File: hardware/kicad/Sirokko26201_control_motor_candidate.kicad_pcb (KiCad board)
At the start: 2 copper layers, 335 x 170 mm, 158 parts, among them J1 DEVKITC1_J1, J10 TC_K_EXHAUST_T+_T-, J102 MOTOR_24V_HIGH_SPEED; 125W_HE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, J11 TC_K_AIR_T+_T-, J12 ROOM_DS18B20_HARNESS, J13 24V_INPUT_PHOENIX_1756993_WIP, J22 START_STOP B3F-4055 + B32-138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, J23 ENCODER EC11E15244G1 + KNOB 4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, J24 RESET NKK BB25AB-FA, J26 TFT CABLE HARWIN M20-9960845 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, J27 GLOW_OUTPUT_PHOENIX_1756993, J28 CLUTCH_OUTPUT_PHOENIX_1756993, J3 DEVKITC1_J3, K1 DG85BM-5021-76-1024 + DZ85AB-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, K2 DG85BM-5021-76-1024 + DZ85AB-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, K3 DG85BM-5021-76-1024 + DZ85AB-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, Q1 IPB017N10N5LFATMA1 WIP, Q101 IRFB4110PBF (100V; RDS(on) @ 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, Q2 IPB017N10N5LFATMA1 WIP, Q20 BC847B,215, Q3 IPB017N10N5LFATMA1 WIP, Q4 IPB017N10N5LFATMA1 WIP, U1 TPS3431SDRBR, U10 MAX31856MUD+, U101 LM5013DDAR, U11 DRV8803PWPR, U13 LM74800QDRRRQ1 WIP_NOT_TRANSI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, U2 SN74HCS74D, U20 SN74LVC1G97DBVR, U301 TPS62162DSGR, U302 TPS3808G33DBVR, U303 74LVC125APW,118 Nexperia ONLY, U6 SN74HCS11D, U9 MAX31856MUD+, U9001 LTC7001IMSE#PBF; MSOP-10 EP, U9002 INA240A1ID, U9003 TLV9020DBVR, U9004 SN74LVC1G32DBVR, U9005 SN74LVC1G08DBVR, U9006 SN74LVC1G08DBVR, U9007 LM317HVT/NOPB TO-220; TJ 0…12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

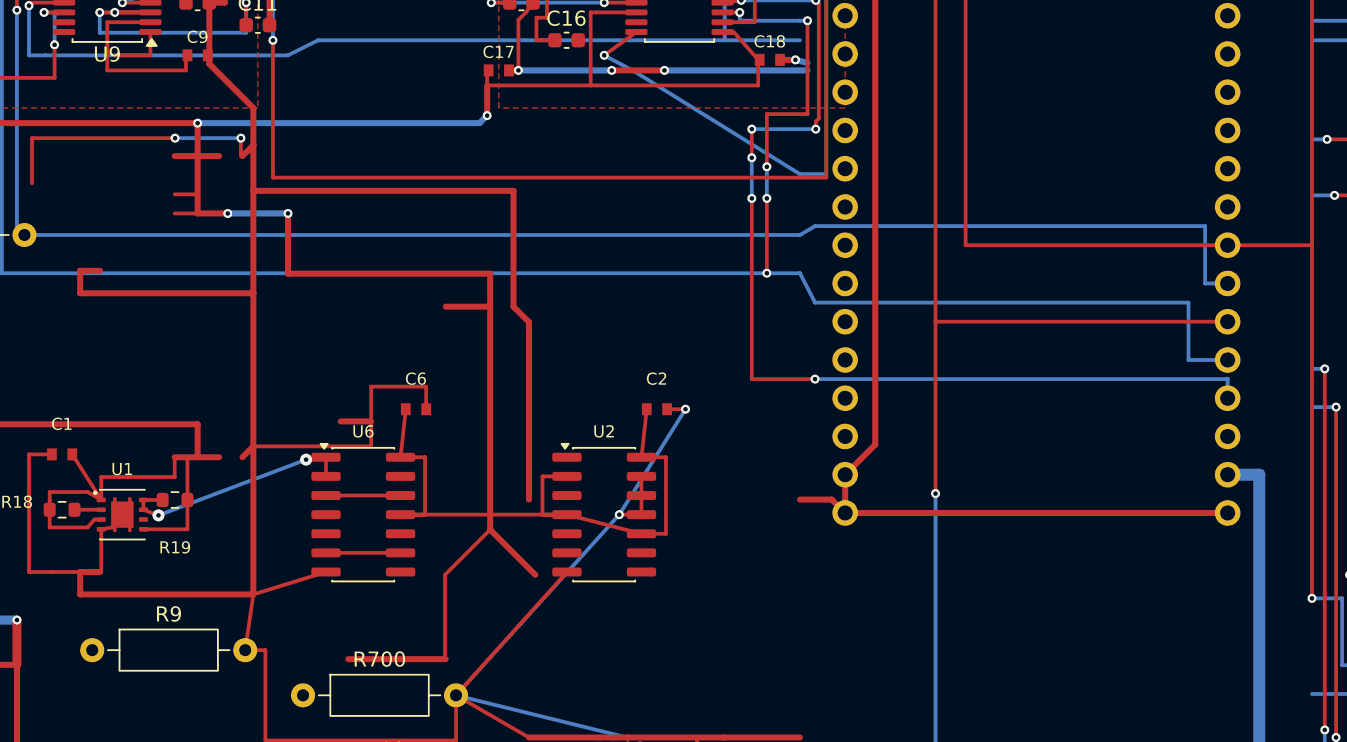
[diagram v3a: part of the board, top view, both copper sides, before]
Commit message: Route WD_HEARTBEAT and CLEAR_N
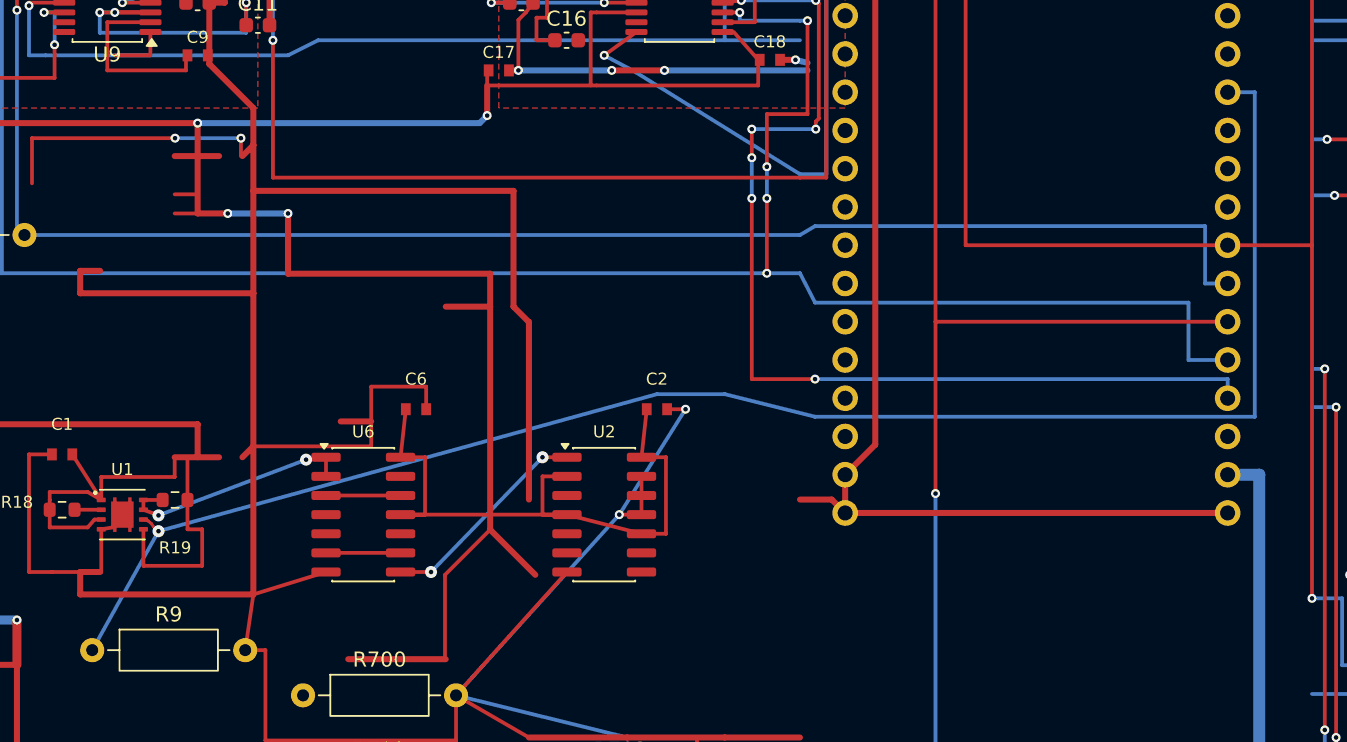
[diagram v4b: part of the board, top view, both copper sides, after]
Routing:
- net /WD_HEARTBEAT: track 0.00 -> 107.9 mm, vias 0 -> 1
- net /MinimalSafety/CLEAR_N: track 0.00 -> 14.3 mm, vias 0 -> 2
- net /+3V3: track 1320.8 -> 1327.6 mm
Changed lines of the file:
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@@
 	)
 	(segment
-		(start 32.4 65.975)
-		(end 35.325 65.975)
-		(width 0.25)
-		(layer "F.Cu")
-		(net "/+3V3")
-	)
-	(segment
 		(start 18 42.77)
 		(end 18 39)
@@
 		(net "/EN_CHIP_PU")
 	)
+	(segment
+		(start 29 74)
+		(end 33.4 66.1)
+		(width 0.25)
+		(layer "B.Cu")
+		(net "/WD_HEARTBEAT")
+	)
+	(segment
+		(start 33.4 66.1)
+		(end 66.5 57)
+		(width 0.25)
+		(layer "B.Cu")
+		(net "/WD_HEARTBEAT")
+	)
+	(segment
+		(start 66.5 57)
+		(end 71 57)
+		(width 0.25)
+		(layer "B.Cu")
+		(net "/WD_HEARTBEAT")
+	)
+	(segment
+		(start 71 57)
+		(end 77 58.5)
+		(width 0.25)
+		(layer "B.Cu")
+		(net "/WD_HEARTBEAT")
+	)
+	(segment
+		(start 77 58.5)
+		(end 106.2 58.5)
+		(width 0.25)
+		(layer "B.Cu")
+		(net "/WD_HEARTBEAT")
+	)
+	(segment
+		(start 106.2 58.5)
+		(end 106.2 36.95)
+		(width 0.25)
+		(layer "B.Cu")
+		(net "/WD_HEARTBEAT")
+	)
+	(segment
+		(start 106.2 36.95)
+		(end 104.4 36.95)
+		(width 0.25)
+		(layer "B.Cu")
+		(net "/WD_HEARTBEAT")
+	)
+	(segment
+		(start 32.4 65.975)
+		(end 32.4 68.4)
+		(width 0.25)
+		(layer "F.Cu")
+		(net "/+3V3")
+	)
+	(segment
+		(start 32.4 68.4)
+		(end 36.3 68.4)
+		(width 0.25)
+		(layer "F.Cu")
+		(net "/+3V3")
+	)
+	(segment
+		(start 36.3 68.4)
+		(end 36.3 65.975)
+		(width 0.25)
+		(layer "F.Cu")
+		(net "/+3V3")
+	)
+	(segment
+		(start 36.3 65.975)
+		(end 35.325 65.975)
+		(width 0.25)
+		(layer "F.Cu")
+		(net "/+3V3")
+	)
+	(segment
+		(start 32.4 65.325)
+		(end 32.72 65.42)
+		(width 0.2)
+		(layer "F.Cu")
+		(net "/WD_HEARTBEAT")
+	)
+	(segment
+		(start 32.72 65.42)
+		(end 32.915465 65.582988)
+		(width 0.2)
+		(layer "F.Cu")
+		(net "/WD_HEARTBEAT")
+	)
+	(segment
+		(start 32.915465 65.582988)
+		(end 33.08 65.82)
+		(width 0.2)
+		(layer "F.Cu")
+		(net "/WD_HEARTBEAT")
+	)
+	(segment
+		(start 33.08 65.82)
+		(end 33.4 66.1)
+		(width 0.2)
+		(layer "F.Cu")
+		(net "/WD_HEARTBEAT")
+	)
+	(via
+		(at 33.4 66.1)
+		(size 0.8)
+		(drill 0.3)
+		(layers "F.Cu" "B.Cu")
+		(net "/WD_HEARTBEAT")
+	)
+	(segment
+		(start 49.475 68.81)
+		(end 51.5 68.81)
+		(width 0.25)
+		(layer "F.Cu")
+		(net "/MinimalSafety/CLEAR_N")
+	)
+	(via
+		(at 51.5 68.81)
+		(size 0.8)
+		(drill 0.3)
+		(layers "F.Cu" "B.Cu")
+		(net "/MinimalSafety/CLEAR_N")
+	)
+	(segment
+		(start 51.5 68.81)
+		(end 58.9 61.19)
+		(width 0.25)
+		(layer "B.Cu")
+		(net "/MinimalSafety/CLEAR_N")
+	)
+	(via
+		(at 58.9 61.19)
+		(size 0.8)
+		(drill 0.3)
+		(layers "F.Cu" "B.Cu")
+		(net "/MinimalSafety/CLEAR_N")
+	)
+	(segment
+		(start 58.9 61.19)
+		(end 60.525 61.19)
+		(width 0.25)
+		(layer "F.Cu")
+		(net "/MinimalSafety/CLEAR_N")
+	)
 	(zone

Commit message: Remove manual RESET from Sirokko WIP
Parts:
- removed J24: RESET NKK BB25AB-FA, Sirokko_Panel:SW_NKK_BB25AB-FA_3D_ENVELOPE
- removed R702: 10k, Resistor_THT:R_Axial_DIN0207_L6.3mm_D2.5mm_P10.16mm_Horizontal
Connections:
- U6 pad 4: /RESET_RELEASED -> /+3V3
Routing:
- net /SAFETY_OK: track 0.00 -> 300.8 mm, vias 0 -> 8
- net /TC_SDI_MOSI: track 191.4 -> 492.0 mm, vias 8 -> 16
- net /MinimalSafety/RELAY_DISABLE: track 0.00 -> 256.4 mm, vias 0 -> 6
- net /GLOW_CMD: track 0.00 -> 228.0 mm, vias 0 -> 6
- net /FUEL_CMD: track 0.00 -> 187.3 mm, vias 0 -> 6
- net /TC_SCK: track 235.7 -> 387.1 mm, vias 8 -> 13
- net /ARM_PULSE: track 0.00 -> 88.0 mm, vias 0 -> 4
- net /MCU_PERMIT: track 0.00 -> 71.9 mm, vias 0 -> 3
- net /MinimalSafety/RELAY_DRIVER_OK: track 0.00 -> 69.6 mm, vias 0 -> 1
- net /GND: track 2212.8 -> 2201.8 mm
- net /TC_SDO_MISO: track 181.9 -> 190.0 mm, vias 9 -> 10
- net /+3V3: track 1327.6 -> 1332.6 mm
- net /INPUT_PROTECTION_WIP_NOT_QUALIFIED/REV_MID: vias 8 -> 9

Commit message: WIP: publish current unfinished CAD sources
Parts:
- removed C1, C2, C6: 100n 16V X7R, Sirokko_TFT_Passives:C_Murata_GRM188_1608_Reflow
- removed R18, R19: 10k 1%, Resistor_SMD:R_0603_1608Metric
- removed R700, R9: 10k, Resistor_THT:R_Axial_DIN0207_L6.3mm_D2.5mm_P10.16mm_Horizontal
- removed R88: 4k7 DRV_IN3_PULLDOWN, Resistor_THT:R_Axial_DIN0207_L6.3mm_D2.5mm_P10.16mm_Horizontal
- removed R89: 10k RELAY_DRIVER_OK_PULLUP, Resistor_THT:R_Axial_DIN0207_L6.3mm_D2.5mm_P10.16mm_Horizontal
- removed U1: TPS3431SDRBR, Sirokko_Safety:TPS3431_DRB0008A_3D
- removed U2: SN74HCS74D, Package_SO:SOIC-14_3.9x8.7mm_P1.27mm
- removed U6: SN74HCS11D, Package_SO:SOIC-14_3.9x8.7mm_P1.27mm
- C103: value 22uF 100V BULK -> 100uF 100V EEU-FR2A101; footprint Capacitor_SMD:C_1210_3225Metric -> Sirokko_Power:CP_Radial_D10.0mm_P5.00mm_Courtyard_D11.0mm
- D9001: footprint Package_TO_SOT_THT:TO-220-3_Vertical -> Sirokko_Power:TO-247-3_Vertical_STPS30H100CW_Drill2.2mm
- moved C103 22.5 mm to (120.0, 35.0)
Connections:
- J1 pad 11: /WD_HEARTBEAT -> unconnected-(J1-Pin_11-Pad11)
- J1 pad 5: /SAFETY_OK -> unconnected-(J1-Pin_5-Pad5)
- J3 pad 7: /ARM_PULSE -> unconnected-(J3-Pin_7-Pad7)
- U11 pad 11: /SAFETY_OK -> /MCU_PERMIT
- U11 pad 16: /MinimalSafety/RELAY_DRIVER_OK -> unconnected-(U11-~{FAULT}-Pad16)
- U11 pad 8: /MinimalSafety/RELAY_DISABLE -> /GND
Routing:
- net /SAFETY_OK: track 300.8 -> 0.00 mm, vias 8 -> 0
- net /MinimalSafety/RELAY_DISABLE: track 256.4 -> 0.00 mm, vias 6 -> 0
- net /START_REQUEST: track 12.5 -> 243.2 mm
- net /MCU_PERMIT: track 71.9 -> 288.3 mm, vias 3 -> 4
- net /TFT_DC: track 0.00 -> 190.1 mm, vias 0 -> 4
- net /+3V3: track 1332.6 -> 1161.3 mm
- net /GND: track 2201.8 -> 2085.9 mm, vias 72 -> 70
- net /WD_HEARTBEAT: track 107.9 -> 0.00 mm, vias 1 -> 0
- net /ENC_B: track 171.7 -> 265.2 mm, vias 15 -> 17
- net /ARM_PULSE: track 88.0 -> 0.00 mm, vias 4 -> 0
- net /MinimalSafety/RELAY_DRIVER_OK: track 69.6 -> 0.00 mm, vias 1 -> 0
- net /ROOM_DQ: track 255.3 -> 288.6 mm, vias 16 -> 17
- net /FAN_REQUEST: track 428.5 -> 460.2 mm, vias 17 -> 18
- net /SPEED_CMD: track 398.7 -> 427.2 mm
- net /MinimalSafety/WD_OK: track 16.1 -> 0.00 mm, vias 2 -> 0
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
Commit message: Update PCB WIP routing snapshot
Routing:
- net /ENC_A: track 142.7 -> 212.9 mm, vias 12 -> 14
- net /ENC_SW: track 71.4 -> 138.0 mm, vias 4 -> 8
- net /TFT_CS: track 283.9 -> 327.1 mm, vias 16 -> 18
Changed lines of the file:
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@@
 		(net "/GND")
 	)
+	(segment
+		(start 79 31.87)
+		(end 82 31.87)
+		(width 0.25)
+		(layer "B.Cu")
+		(net "/ENC_A")
+	)
+	(via
+		(at 82 31.87)
+		(size 0.6)
+		(drill 0.3)
+		(layers "F.Cu" "B.Cu")
+		(net "/ENC_A")
+	)
+	(segment
+		(start 82 31.87)
+		(end 82 62.7)
+		(width 0.25)
+		(layer "F.Cu")
+		(net "/ENC_A")
+	)
+	(via
+		(at 82 62.7)
+		(size 0.6)
+		(drill 0.3)
+		(layers "F.Cu" "B.Cu")
+		(net "/ENC_A")
+	)
+	(segment
+		(start 82 62.7)
+		(end 90 62.7)
+		(width 0.25)
+		(layer "B.Cu")
+		(net "/ENC_A")
+	)
+	(segment
+		(start 90 62.7)
+		(end 90 91)
+		(width 0.25)
+		(layer "B.Cu")
+		(net "/ENC_A")
+	)
+	(segment
+		(start 79 34.41)
+		(end 83 34.41)
+		(width 0.25)
+		(layer "B.Cu")
+		(net "/ENC_SW")
+	)
+	(via
+		(at 83 34.41)
+		(size 0.6)
+		(drill 0.3)
+		(layers "F.Cu" "B.Cu")
+		(net "/ENC_SW")
+	)
+	(segment
+		(start 83 34.41)
+		(end 83 63.8)
+		(width 0.25)
+		(layer "F.Cu")
+		(net "/ENC_SW")
+	)
+	(via
+		(at 83 63.8)
+		(size 0.6)
+		(drill 0.3)
+		(layers "F.Cu" "B.Cu")
+		(net "/ENC_SW")
+	)
+	(segment
+		(start 83 63.8)
+		(end 83 66)
+		(width 0.25)
+		(layer "B.Cu")
+		(net "/ENC_SW")
+	)
+	(via
+		(at 83 66)
+		(size 0.6)
+		(drill 0.3)
+		(layers "F.Cu" "B.Cu")
+		(net "/ENC_SW")
+	)
+	(segment
+		(start 83 66)
+		(end 83 84)
+		(width 0.25)
+		(layer "F.Cu")
+		(net "/ENC_SW")
+	)
+	(via
+		(at 83 84)
+		(size 0.6)
+		(drill 0.3)
+		(layers "F.Cu" "B.Cu")
+		(net "/ENC_SW")
+	)
+	(segment
+		(start 83 84)
+		(end 89 84)
+		(width 0.25)
+		(layer "B.Cu")
+		(net "/ENC_SW")
+	)
+	(segment
+		(start 89 84)
+		(end 89 91)
+		(width 0.25)
+		(layer "B.Cu")
+		(net "/ENC_SW")
+	)
+	(segment
+		(start 79 52.19)
+		(end 80.2 53.39)
+		(width 0.25)
+		(layer "F.Cu")
+		(net "/TFT_CS")
+	)
+	(segment
+		(start 80.2 53.39)
+		(end 80.2 58.4)
+		(width 0.25)
+		(layer "F.Cu")
+		(net "/TFT_CS")
+	)
+	(via
+		(at 80.2 58.4)
+		(size 0.6)
+		(drill 0.3)
+		(layers "F.Cu" "B.Cu")
+		(net "/TFT_CS")
+	)
+	(segment
+		(start 80.2 58.4)
+		(end 80.2 66.5)
+		(width 0.25)
+		(layer "B.Cu")
+		(net "/TFT_CS")
+	)
+	(via
+		(at 80.2 66.5)
+		(size 0.6)
+		(drill 0.3)
+		(layers "F.Cu" "B.Cu")
+		(net "/TFT_CS")
+	)
+	(segment
+		(start 80.2 66.5)
+		(end 80.2 93.2)
+		(width 0.25)
+		(layer "F.Cu")
+		(net "/TFT_CS")
+	)
+	(segment
+		(start 80.2 93.2)
+		(end 79.4 94)
+		(width 0.25)
+		(layer "F.Cu")
+		(net "/TFT_CS")
+	)
+	(segment
+		(start 79.4 94)
+		(end 78.8 94)
+		(width 0.25)
+		(layer "F.Cu")
+		(net "/TFT_CS")
+	)
 )

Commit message: Update +3V3 PCB WIP routing snapshot
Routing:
- net /+3V3: track 1161.3 -> 1188.7 mm, vias 36 -> 38
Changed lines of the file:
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@@
 		(net "/TFT_CS")
 	)
+	(segment
+		(start 26.8 104.975)
+		(end 27.775 104)
+		(width 0.3)
+		(layer "F.Cu")
+		(net "/+3V3")
+	)
+	(segment
+		(start 27.775 104)
+		(end 27.775 102)
+		(width 0.3)
+		(layer "F.Cu")
+		(net "/+3V3")
+	)
+	(via
+		(at 27.775 103)
+		(size 0.6)
+		(drill 0.3)
+		(layers "F.Cu" "B.Cu")
+		(net "/+3V3")
+	)
+	(segment
+		(start 33.4 108.975)
+		(end 30.775 106.35)
+		(width 0.4)
+		(layer "F.Cu")
+		(net "/+3V3")
+	)
+	(segment
+		(start 30.775 106.35)
+		(end 30.775 103)
+		(width 0.4)
+		(layer "F.Cu")
+		(net "/+3V3")
+	)
+	(segment
+		(start 35.225 92)
+		(end 35.225 98.3)
+		(width 0.3)
+		(layer "B.Cu")
+		(net "/+3V3")
+	)
+	(via
+		(at 35.225 92)
+		(size 0.6)
+		(drill 0.3)
+		(layers "F.Cu" "B.Cu")
+		(net "/+3V3")
+	)
+	(segment
+		(start 24 87.7)
+		(end 28.3 92)
+		(width 0.4)
+		(layer "F.Cu")
+		(net "/+3V3")
+	)
+	(segment
+		(start 28.3 92)
+		(end 32.9375 92)
+		(width 0.4)
+		(layer "F.Cu")
+		(net "/+3V3")
+	)
 )
